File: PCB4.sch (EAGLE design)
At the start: 40 parts

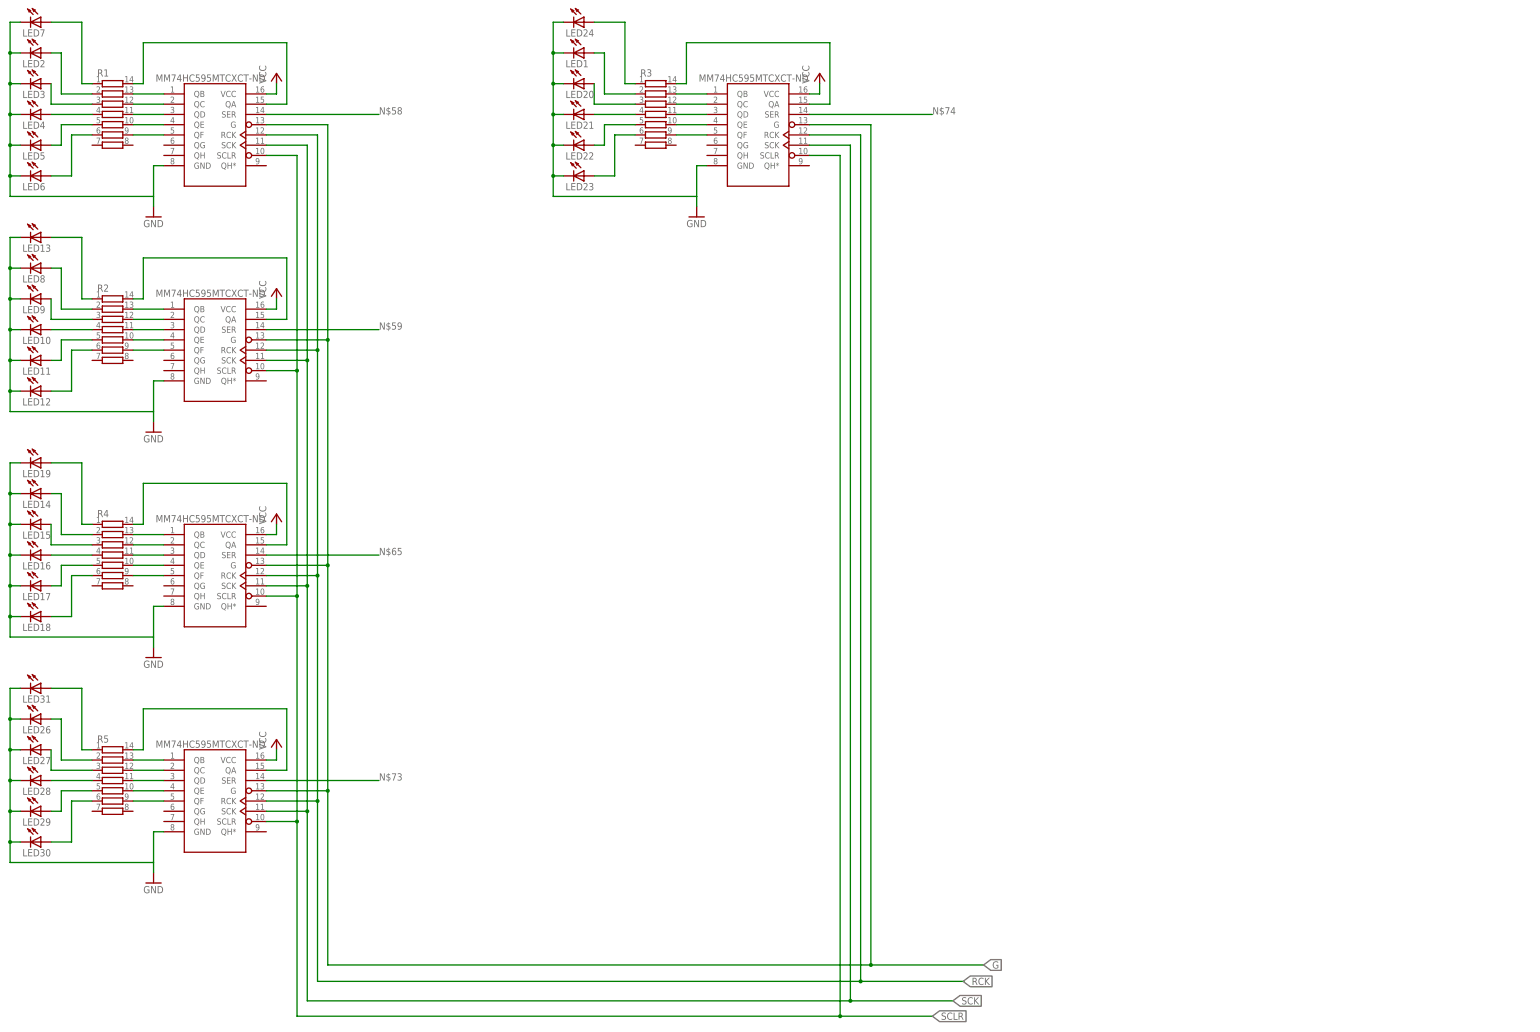
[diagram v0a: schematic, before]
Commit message: Fixed library issue where library won't load. Added jumpers and resistor arrays to PCB4
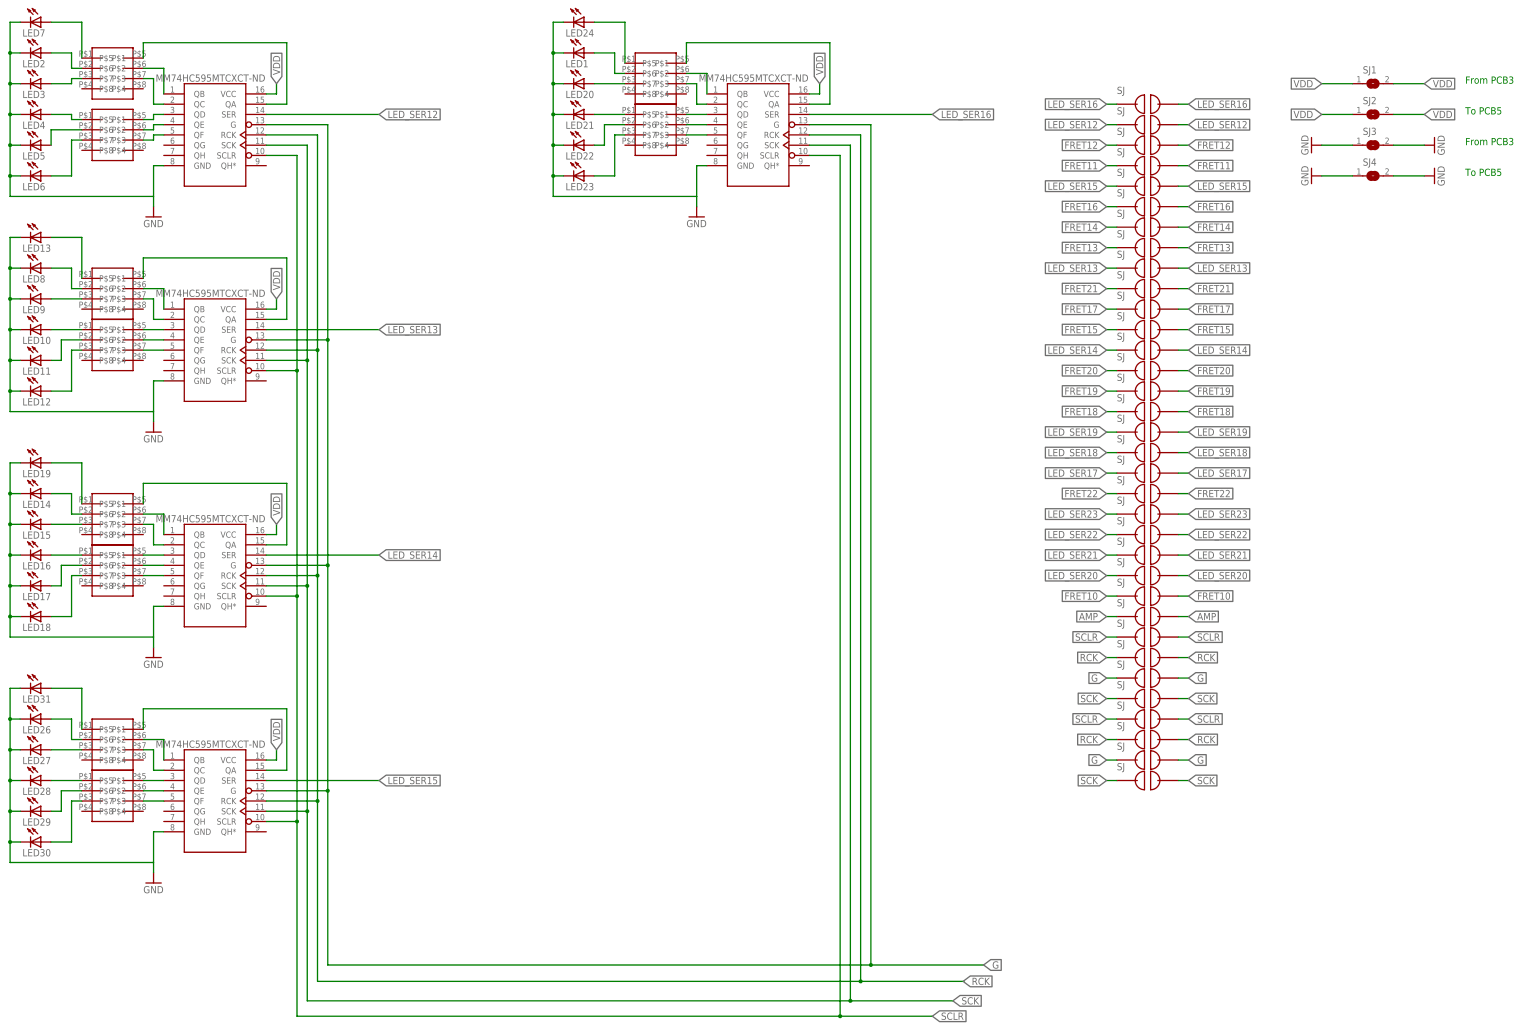
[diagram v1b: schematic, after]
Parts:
- removed R1, R2, R3, R4, R5: (no value), resistor-bourns:4814P-T01
- added SJ1, SJ2, SJ3, SJ4: (no value), jumper:SJ
- added U$10, U$11, U$12, U$13, U$14, U$15, U$6, U$7, U$8, U$9: MNR04MRAPJ680, ECE477_Guitutar:MNR04MRAPJ680
- added U$19, U$42, U$45, U$46, U$47, U$48, U$49, U$50, U$51, U$52, U$53, U$54, U$55, U$56, U$57, U$58, U$59, U$60, U$61, U$62, U$63, U$64, U$65, U$66, U$67, U$68, U$69, U$70, U$79, U$80, U$81, U$82, U$83, U$84: JUMPER, ECE477_Guitutar:JUMPER
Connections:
- removed net N$58: U$4.SER
- removed net N$59: U$1.SER
- removed net N$62: R5.11, U$5.QD
- removed net N$63: R5.10, U$5.QE
- removed net N$64: R5.9, U$5.QF
- removed net N$65: U$3.SER
- removed net N$67: LED31.A, R5.1
- removed net N$68: LED26.A, R5.2
- removed net N$69: LED27.A, R5.3
- removed net N$70: LED28.A, R5.4
- removed net N$71: LED29.A, R5.5
- removed net N$72: LED30.A, R5.6
- removed net N$73: U$5.SER
- removed net N$74: U$2.SER
- removed net VCC: U$1.VCC, U$2.VCC, U$3.VCC, U$4.VCC, U$5.VCC
- new net AMP: U$70.P$1, U$70.P$2
- new net FRET10: U$69.P$1, U$69.P$2
- new net FRET11: U$48.P$1, U$48.P$2
- new net FRET12: U$47.P$1, U$47.P$2
- new net FRET13: U$52.P$1, U$52.P$2
- new net FRET14: U$51.P$1, U$51.P$2
- new net FRET15: U$56.P$1, U$56.P$2
- new net FRET16: U$50.P$1, U$50.P$2
- new net FRET17: U$55.P$1, U$55.P$2
- new net FRET18: U$60.P$1, U$60.P$2
- new net FRET19: U$59.P$1, U$59.P$2
- new net FRET20: U$58.P$1, U$58.P$2
- new net FRET21: U$54.P$1, U$54.P$2
- new net FRET22: U$64.P$1, U$64.P$2
- new net LED_SER12: U$4.SER, U$46.P$1, U$46.P$2
- new net LED_SER13: U$1.SER, U$53.P$1, U$53.P$2
- new net LED_SER14: U$3.SER, U$57.P$1, U$57.P$2
- new net LED_SER15: U$49.P$1, U$49.P$2, U$5.SER
- new net LED_SER16: U$2.SER, U$45.P$1, U$45.P$2
- new net LED_SER17: U$63.P$1, U$63.P$2
- new net LED_SER18: U$62.P$1, U$62.P$2
- new net LED_SER19: U$61.P$1, U$61.P$2
- new net LED_SER20: U$68.P$1, U$68.P$2
- new net LED_SER21: U$67.P$1, U$67.P$2
- new net LED_SER22: U$66.P$1, U$66.P$2
- new net LED_SER23: U$65.P$1, U$65.P$2
- new net N$13: LED13.A, U$8.P$1
- new net N$17: LED9.A, U$8.P$3
- new net N$18: LED10.A, U$9.P$1
- new net N$31: U$11.P$5, U$3.QD
- new net N$33: U$11.P$7, U$3.QF
- new net N$34: LED18.A, U$11.P$3
- new net N$50: LED1.A, U$14.P$2
- new net N$53: U$14.P$7, U$2.QC
- new net N$54: U$15.P$5, U$2.QD
- new net VDD: SJ1.1, SJ1.2, SJ2.1, SJ2.2, U$1.VCC, U$2.VCC, U$3.VCC, U$4.VCC, U$5.VCC
- net G: now also U$80.P$1, U$80.P$2, U$84.P$1, U$84.P$2
- net GND: now also SJ3.1, SJ3.2, SJ4.1, SJ4.2
- net N$1: now also LED2.A, U$6.P$2; no longer R1.13, U$4.QB
- net N$10: now also U$4.QE, U$7.P$6; no longer LED4.A, R1.4
- net N$11: now also U$4.QF, U$7.P$7; no longer LED5.A, R1.5
- net N$12: now also U$7.P$3; no longer R1.6
- net N$14: now also LED8.A, U$8.P$2; no longer R3.13, U$2.QB
- net N$15: now also U$1.QB, U$8.P$6; no longer R3.12, U$2.QC
- net N$16: now also U$1.QC, U$8.P$7; no longer R3.11, U$2.QD
- net N$19: now also U$1.QD, U$9.P$5; no longer R2.13, U$1.QB
- net N$2: now also U$4.QB, U$6.P$6; no longer R1.12, U$4.QC
- net N$20: now also LED11.A, U$9.P$2; no longer R2.12, U$1.QC
- net N$21: now also U$1.QE, U$9.P$6; no longer R2.11, U$1.QD
- net N$22: now also U$1.QF, U$9.P$7; no longer R2.10, U$1.QE
- net N$23: now also LED12.A, U$9.P$3; no longer R2.9, U$1.QF
- net N$24: now also U$8.P$5; no longer R2.14
- net N$25: now also LED19.A, U$10.P$1; no longer LED13.A, R2.1
- net N$26: now also LED14.A, U$10.P$2; no longer LED8.A, R2.2
- net N$27: now also U$10.P$6, U$3.QB; no longer LED9.A, R2.3
- net N$28: now also U$10.P$7, U$3.QC; no longer LED10.A, R2.4
- net N$29: now also LED15.A, U$10.P$3; no longer LED11.A, R2.5
- net N$3: now also LED3.A, U$6.P$3; no longer R1.11, U$4.QD
- net N$30: now also LED16.A, U$11.P$1; no longer LED12.A, R2.6
- net N$32: now also U$11.P$6, U$3.QE; no longer R3.10, U$2.QE
- net N$35: now also LED17.A, U$11.P$2; no longer R4.13, U$3.QB
- net N$36: now also LED31.A, U$12.P$1; no longer R4.12, U$3.QC
- net N$37: now also LED26.A, U$12.P$2; no longer R4.11, U$3.QD
- net N$38: now also LED27.A, U$12.P$3; no longer R4.10, U$3.QE
- net N$39: now also U$12.P$7, U$5.QC; no longer R4.9, U$3.QF
- net N$4: now also U$4.QC, U$6.P$7; no longer R1.10, U$4.QE
- net N$40: now also U$10.P$5; no longer R4.14
- net N$41: now also U$12.P$6, U$5.QB; no longer LED19.A, R4.1
- net N$42: now also U$13.P$5, U$5.QD; no longer R3.9, U$2.QF
- net N$43: now also U$13.P$6, U$5.QE; no longer LED14.A, R4.2
- net N$44: now also U$13.P$7, U$5.QF; no longer LED15.A, R4.3
- net N$45: now also U$14.P$5; no longer R3.14
- net N$46: now also LED28.A, U$13.P$1; no longer LED16.A, R4.4
- net N$47: now also LED29.A, U$13.P$2; no longer LED17.A, R4.5
- net N$48: now also LED30.A, U$13.P$3; no longer LED24.A, R3.1
- net N$49: now also LED24.A, U$14.P$1; no longer LED18.A, R4.6
- net N$5: now also LED4.A, U$7.P$1; no longer R1.9, U$4.QF
- net N$51: now also LED20.A, U$14.P$3; no longer LED1.A, R3.2
- net N$52: now also U$14.P$6, U$2.QB; no longer LED20.A, R3.3
- net N$55: now also U$15.P$6, U$2.QE; no longer LED21.A, R3.4
- net N$56: now also U$15.P$7, U$2.QF; no longer LED22.A, R3.5
- net N$57: now also U$15.P$3; no longer R3.6
- net N$6: now also U$6.P$1; no longer R1.1
- net N$60: now also LED22.A, U$15.P$2; no longer R5.13, U$5.QB
- net N$61: now also LED21.A, U$15.P$1; no longer R5.12, U$5.QC
- net N$66: now also U$12.P$5; no longer R5.14
- net N$7: now also U$6.P$5; no longer R1.14
- net N$8: now also LED5.A, U$7.P$2; no longer LED2.A, R1.2
- net N$9: now also U$4.QD, U$7.P$5; no longer LED3.A, R1.3
- net RCK: now also U$79.P$1, U$79.P$2, U$83.P$1, U$83.P$2
- net SCK: now also U$42.P$1, U$42.P$2, U$81.P$1, U$81.P$2
- net SCLR: now also U$19.P$1, U$19.P$2, U$82.P$1, U$82.P$2
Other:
- note added: "From PCB3"
- note added: "To PCB5"

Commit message: Finished PCB4. Finished gerbers for PCB1, 2, 3, and 4
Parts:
- removed U$70: JUMPER, ECE477_Guitutar:JUMPER
- added FRET10, FRET11, FRET12, FRET13, FRET14: (no value), wirepad:2,54/0,9
- added H1, H2: MOUNT-HOLE2.8, holes:MOUNT-HOLE2.8
- added R28: 330k, rcl:R-US_R0805
- added R29, R30, R31, R32: (no value), rcl:R-US_R0805
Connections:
- removed net AMP: U$70.P$1, U$70.P$2
- removed net GND1: LED1.C, LED20.C, LED21.C, LED22.C, LED23.C, LED24.C, U$2.GND
- new net N$58: FRET10.P, R28.1
- new net N$59: FRET11.P, R29.1
- new net N$62: FRET12.P, R30.1
- new net N$63: FRET13.P, R31.1
- new net N$64: FRET14.P, R32.1
- net FRET10: now also R28.2
- net FRET11: now also R29.2
- net FRET12: now also R30.2
- net FRET13: now also R31.2
- net FRET14: now also R32.2
- net GND: now also LED1.C, LED20.C, LED21.C, LED22.C, LED23.C, LED24.C, U$2.GND
